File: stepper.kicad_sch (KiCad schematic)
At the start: 10 parts, among them M3 Stepper_Motor_bipolar, U2 DRV8424RGER

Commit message: schem: set stepper driver microstepping and decay config
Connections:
- net +3V3: now also U2.13 (M0)
- net GND: now also U2.15 (DECAY1), U2.16 (DECAY0)
- no-connect marks 0 -> 2
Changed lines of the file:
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@@
+	)
+	(junction
+		(at 161.29 113.03)
+		(diameter 0)
+		(color 0 0 0 0)
 	)
 	(junction
@@
 		(color 0 0 0 0)
 	)
+	(no_connect
+		(at 160.02 107.95)
+	)
+	(no_connect
+		(at 134.62 110.49)
+	)
 	(wire
 		(pts
@@
 	(wire
 		(pts
+			(xy 161.29 114.3) (xy 161.29 113.03)
+		)
+		(stroke
+			(width 0)
+			(type default)
+		)
+	)
+	(wire
+		(pts
 			(xy 125.73 91.44) (xy 125.73 92.71)
 		)
@@
 	(wire
 		(pts
+			(xy 134.62 107.95) (xy 125.73 107.95)
+		)
+		(stroke
+			(width 0)
+			(type default)
+		)
+	)
+	(wire
+		(pts
 			(xy 128.27 104.14) (xy 134.62 104.14)
 		)
@@
 	(wire
 		(pts
+			(xy 161.29 110.49) (xy 161.29 113.03)
+		)
+		(stroke
+			(width 0)
+			(type default)
+		)
+	)
+	(wire
+		(pts
 			(xy 160.02 105.41) (xy 165.1 105.41)
 		)
@@
 	(wire
 		(pts
+			(xy 125.73 107.95) (xy 125.73 106.68)
+		)
+		(stroke
+			(width 0)
+			(type default)
+		)
+	)
+	(wire
+		(pts
 			(xy 160.02 99.06) (xy 162.56 99.06)
 		)
@@
 	(wire
 		(pts
+			(xy 161.29 113.03) (xy 160.02 113.03)
+		)
+		(stroke
+			(width 0)
+			(type default)
+		)
+	)
+	(wire
+		(pts
 			(xy 146.05 80.01) (xy 146.05 78.74)
 		)
@@
 		(pts
 			(xy 172.72 101.6) (xy 172.72 99.06)
+		)
+		(stroke
+			(width 0)
+			(type default)
+		)
+	)
+	(wire
+		(pts
+			(xy 160.02 110.49) (xy 161.29 110.49)
 		)
 		(stroke
@@
 	)
 	(symbol
+		(lib_id "power:GND")
+		(at 161.29 114.3 0)
+		(mirror y)
+		(unit 1)
+		(exclude_from_sim no)
+		(in_bom yes)
+		(on_board yes)
+		(dnp no)
+		(property "Reference" "#PWR066"
+			(at 161.29 120.65 0)
+			(effects
+				(font
+					(size 1.27 1.27)
+				)
+				(hide yes)
+			)
+		)
+		(property "Value" "GND"
+			(at 165.354 115.824 0)
+			(effects
+				(font
+					(size 1.27 1.27)
+				)
+				(hide yes)
+			)
+		)
+		(property "Footprint" ""
+			(at 161.29 114.3 0)
+			(effects
+				(font
+					(size 1.27 1.27)
+				)
+				(hide yes)
+			)
+		)
+		(property "Datasheet" ""
+			(at 161.29 114.3 0)
+			(effects
+				(font
+					(size 1.27 1.27)
+				)
+				(hide yes)
+			)
+		)
+		(property "Description" "Power symbol creates a global label with name \"GND\" , ground"
+			(at 161.29 114.3 0)
+			(effects
+				(font
+					(size 1.27 1.27)
+				)
+				(hide yes)
+			)
+		)
+		(pin "1"
+		)
+		(instances
+			(project "valrob-pami-cdf-1"
+				(path "/453def7e-2a78-4c3c-a4b7-f12883e5bdd2/ac36a521-9363-451f-b288-e4e7fa573403"
+					(reference "#PWR066")
+					(unit 1)
+				)
+			)
+		)
+	)
+	(symbol
 		(lib_id "Device:C_Polarized")
 		(at 163.83 80.01 0)
@@
 					(unit 1)
 				)
+			)
+		)
+	)
+	(symbol
+		(lib_id "power:+3V3")
+		(at 125.73 106.68 0)
+		(unit 1)
+		(exclude_from_sim no)
+		(in_bom yes)
+		(on_board yes)
+		(dnp no)
+		(property "Reference" "#PWR061"
+			(at 125.73 110.49 0)
+			(effects
+				(font
+					(size 1.27 1.27)
+				)
+				(hide yes)
+			)
+		)
+		(property "Value" "+3V3"
+			(at 121.666 104.902 0)
+			(effects
+				(font
+					(size 1.27 1.27)
+				)
+			)
+		)
+		(property "Footprint" ""
+			(at 125.73 106.68 0)
+			(effects
+				(font
+					(size 1.27 1.27)
+				)
+				(hide yes)
+			)
+		)
+		(property "Datasheet" ""
+			(at 125.73 106.68 0)
+			(effects
+				(font
+					(size 1.27 1.27)
+				)
+				(hide yes)
+			)
+		)
+		(property "Description" "Power symbol creates a global label with name \"+3V3\""
+			(at 125.73 106.68 0)
+			(effects
+				(font
+					(size 1.27 1.27)
+				)
+				(hide yes)
+			)
+		)
+		(pin "1"
+		)
+		(instances
+			(project "valrob-pami-cdf-1"
+				(path "/453def7e-2a78-4c3c-a4b7-f12883e5bdd2/ac36a521-9363-451f-b288-e4e7fa573403"
+					(reference "#PWR061")
+					(unit 1)
+				)

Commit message: schem: change stepper driver connector
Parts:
- M3: footprint GLCS:JST_XH_S6B-XH-A_Stepper_1x06_P2.50mm_Horizontal -> Connector_JST:JST_XH_B4B-XH-A_1x04_P2.50mm_Vertical
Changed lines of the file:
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@@
 			)
 		)
-		(property "Footprint" "GLCS:JST_XH_S6B-XH-A_Stepper_1x06_P2.50mm_Horizontal"
+		(property "Footprint" "Connector_JST:JST_XH_B4B-XH-A_1x04_P2.50mm_Vertical"
 			(at 170.434 91.186 0)
 			(effects

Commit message: schem: fix stepper hierachical sheets
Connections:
- net ~{FAULT}: now reaches R19.1, U2.11 (~{FAULT})
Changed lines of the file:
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@@
+	)
+	(junction
+		(at 125.73 101.6)
+		(diameter 0)
+		(color 0 0 0 0)
 	)
 	(junction
@@
 	(wire
 		(pts
+			(xy 124.46 101.6) (xy 125.73 101.6)
+		)
+		(stroke
+			(width 0)
+			(type default)
+		)
+	)
+	(wire
+		(pts
 			(xy 147.32 123.19) (xy 147.32 124.46)
 		)
@@
 	(wire
 		(pts
-			(xy 129.54 93.98) (xy 134.62 93.98)
-		)
-		(stroke
-			(width 0)
-			(type default)
-		)
-	)
-	(wire
-		(pts
 			(xy 161.29 88.9) (xy 161.29 91.44)
 		)
@@
 	(wire
 		(pts
+			(xy 133.35 91.44) (xy 134.62 91.44)
+		)
+		(stroke
+			(width 0)
+			(type default)
+		)
+	)
+	(wire
+		(pts
 			(xy 163.83 96.52) (xy 160.02 96.52)
 		)
@@
 	(wire
 		(pts
-			(xy 128.27 104.14) (xy 134.62 104.14)
-		)
-		(stroke
-			(width 0)
-			(type default)
-		)
-	)
-	(wire
-		(pts
-			(xy 129.54 96.52) (xy 134.62 96.52)
-		)
-		(stroke
-			(width 0)
-			(type default)
-		)
-	)
-	(wire
-		(pts
 			(xy 167.64 105.41) (xy 167.64 106.68)
 		)
@@
 	(wire
 		(pts
+			(xy 133.35 93.98) (xy 134.62 93.98)
+		)
+		(stroke
+			(width 0)
+			(type default)
+		)
+	)
+	(wire
+		(pts
 			(xy 161.29 110.49) (xy 161.29 113.03)
 		)
@@
 	(wire
 		(pts
+			(xy 133.35 96.52) (xy 134.62 96.52)
+		)
+		(stroke
+			(width 0)
+			(type default)
+		)
+	)
+	(wire
+		(pts
 			(xy 148.59 74.93) (xy 153.67 74.93)
 		)
@@
 	(wire
 		(pts
-			(xy 176.53 105.41) (xy 182.88 105.41)
-		)
-		(stroke
-			(width 0)
-			(type default)
-		)
-	)
-	(wire
-		(pts
-			(xy 129.54 91.44) (xy 134.62 91.44)
+			(xy 176.53 105.41) (xy 179.07 105.41)
 		)
 		(stroke
@@
 		)
 	)
-	(label "STEP"
-		(at 129.54 91.44 0)
+	(hierarchical_label "~{SLEEP}"
+		(shape input)
+		(at 134.62 104.14 180)
 		(effects
 			(font
 				(size 1.27 1.27)
 			)
-			(justify left bottom)
-		)
-	)
-	(label "~{SLEEP}"
-		(at 128.27 104.14 0)
+			(justify right)
+		)
+	)
+	(hierarchical_label "DIR"
+		(shape input)
+		(at 133.35 93.98 180)
 		(effects
 			(font
 				(size 1.27 1.27)
 			)
-			(justify left bottom)
-		)
-	)
-	(label "VPWM"
-		(at 182.88 105.41 180)
+			(justify right)
+		)
+	)
+	(hierarchical_label "STEP"
+		(shape input)
+		(at 133.35 91.44 180)
 		(effects
 			(font
 				(size 1.27 1.27)
 			)
-			(justify right bottom)
-		)
-	)
-	(label "EN"
-		(at 129.54 96.52 0)
+			(justify right)
+		)
+	)
+	(hierarchical_label "~{FAULT}"
+		(shape output)
+		(at 124.46 101.6 180)
 		(effects
 			(font
 				(size 1.27 1.27)
 			)
-			(justify left bottom)
-		)
-	)
-	(label "DIR"
-		(at 129.54 93.98 0)
+			(justify right)
+		)
+	)
+	(hierarchical_label "EN"
+		(shape input)
+		(at 133.35 96.52 180)
 		(effects
 			(font
 				(size 1.27 1.27)
 			)
-			(justify left bottom)
+			(justify right)
+		)
+	)
+	(hierarchical_label "VPWM"
+		(shape input)
+		(at 179.07 105.41 0)
+		(effects
+			(font
+				(size 1.27 1.27)
+			)
+			(justify left)
 		)
 	)
@@
 				(path "/453def7e-2a78-4c3c-a4b7-f12883e5bdd2/ac36a521-9363-451f-b288-e4e7fa573403"
 					(reference "#PWR049")
+					(unit 1)
+				)
+				(path "/453def7e-2a78-4c3c-a4b7-f12883e5bdd2/da99261a-b7a2-4c14-91bb-816ce46ae8f8"
+					(reference "#PWR077")
 					(unit 1)
 				)
@@
 					(unit 1)
 				)
+				(path "/453def7e-2a78-4c3c-a4b7-f12883e5bdd2/da99261a-b7a2-4c14-91bb-816ce46ae8f8"
+					(reference "C40")
+					(unit 1)
+				)
 			)
 		)
@@
 					(unit 1)
 				)
+				(path "/453def7e-2a78-4c3c-a4b7-f12883e5bdd2/da99261a-b7a2-4c14-91bb-816ce46ae8f8"
+					(reference "#PWR074")
+					(unit 1)
+				)
 			)
 		)
@@
 					(unit 1)
 				)
+				(path "/453def7e-2a78-4c3c-a4b7-f12883e5bdd2/da99261a-b7a2-4c14-91bb-816ce46ae8f8"
+					(reference "C39")
+					(unit 1)
+				)
 			)
 		)
@@
 					(unit 1)
 				)
+				(path "/453def7e-2a78-4c3c-a4b7-f12883e5bdd2/da99261a-b7a2-4c14-91bb-816ce46ae8f8"
+					(reference "#PWR069")
+					(unit 1)
+				)
 			)
 		)
@@
 					(unit 1)
 				)
+				(path "/453def7e-2a78-4c3c-a4b7-f12883e5bdd2/da99261a-b7a2-4c14-91bb-816ce46ae8f8"
+					(reference "M2")
+					(unit 1)
+				)
 			)
 		)
@@
 					(unit 1)
 				)
+				(path "/453def7e-2a78-4c3c-a4b7-f12883e5bdd2/da99261a-b7a2-4c14-91bb-816ce46ae8f8"
+					(reference "#PWR072")
+					(unit 1)
+				)
 			)
 		)
@@
 				(path "/453def7e-2a78-4c3c-a4b7-f12883e5bdd2/ac36a521-9363-451f-b288-e4e7fa573403"
 					(reference "#PWR01")
+					(unit 1)
+				)
+				(path "/453def7e-2a78-4c3c-a4b7-f12883e5bdd2/da99261a-b7a2-4c14-91bb-816ce46ae8f8"
+					(reference "#PWR067")
 					(unit 1)
 				)
@@
 				(path "/453def7e-2a78-4c3c-a4b7-f12883e5bdd2/ac36a521-9363-451f-b288-e4e7fa573403"
 					(reference "#PWR023")
+					(unit 1)
+				)
+				(path "/453def7e-2a78-4c3c-a4b7-f12883e5bdd2/da99261a-b7a2-4c14-91bb-816ce46ae8f8"
+					(reference "#PWR073")
 					(unit 1)
 				)
@@
 					(unit 1)
 				)
+				(path "/453def7e-2a78-4c3c-a4b7-f12883e5bdd2/da99261a-b7a2-4c14-91bb-816ce46ae8f8"
+					(reference "R33")
+					(unit 1)
+				)
 			)
 		)
@@
 					(unit 1)
 				)
+				(path "/453def7e-2a78-4c3c-a4b7-f12883e5bdd2/da99261a-b7a2-4c14-91bb-816ce46ae8f8"
+					(reference "#FLG08")
+					(unit 1)
+				)
 			)
 		)
@@
 					(unit 1)
 				)
+				(path "/453def7e-2a78-4c3c-a4b7-f12883e5bdd2/da99261a-b7a2-4c14-91bb-816ce46ae8f8"
+					(reference "C36")
+					(unit 1)
+				)
 			)
 		)
@@
 					(unit 1)
 				)
+				(path "/453def7e-2a78-4c3c-a4b7-f12883e5bdd2/da99261a-b7a2-4c14-91bb-816ce46ae8f8"
+					(reference "#PWR075")
+					(unit 1)
+				)
 			)
 		)
@@
 				(path "/453def7e-2a78-4c3c-a4b7-f12883e5bdd2/ac36a521-9363-451f-b288-e4e7fa573403"
 					(reference "C30")
+					(unit 1)
+				)
+				(path "/453def7e-2a78-4c3c-a4b7-f12883e5bdd2/da99261a-b7a2-4c14-91bb-816ce46ae8f8"
+					(reference "C37")
 					(unit 1)
 				)
@@
 					(unit 1)
 				)
+				(path "/453def7e-2a78-4c3c-a4b7-f12883e5bdd2/da99261a-b7a2-4c14-91bb-816ce46ae8f8"
+					(reference "#PWR076")
+					(unit 1)
+				)
 			)
 		)
@@
 					(unit 1)
 				)
+				(path "/453def7e-2a78-4c3c-a4b7-f12883e5bdd2/da99261a-b7a2-4c14-91bb-816ce46ae8f8"
+					(reference "C35")
+					(unit 1)
+				)
 			)
 		)
@@
 					(unit 1)
 				)
+				(path "/453def7e-2a78-4c3c-a4b7-f12883e5bdd2/da99261a-b7a2-4c14-91bb-816ce46ae8f8"
+					(reference "C38")
+					(unit 1)
+				)
 			)
 		)
@@
 					(unit 1)
 				)
+				(path "/453def7e-2a78-4c3c-a4b7-f12883e5bdd2/da99261a-b7a2-4c14-91bb-816ce46ae8f8"
+					(reference "U6")
+					(unit 1)
+				)
 			)
 		)
@@
 					(unit 1)
 				)
+				(path "/453def7e-2a78-4c3c-a4b7-f12883e5bdd2/da99261a-b7a2-4c14-91bb-816ce46ae8f8"
+					(reference "R34")
+					(unit 1)
+				)

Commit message: schem: reannotate
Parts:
- renumbered C28 to C35, C29 to C36, C30 to C37, C31 to C38, C32 to C39, C33 to C40, M3 to M2, R19 to R36, R27 to R37, U2 to U6

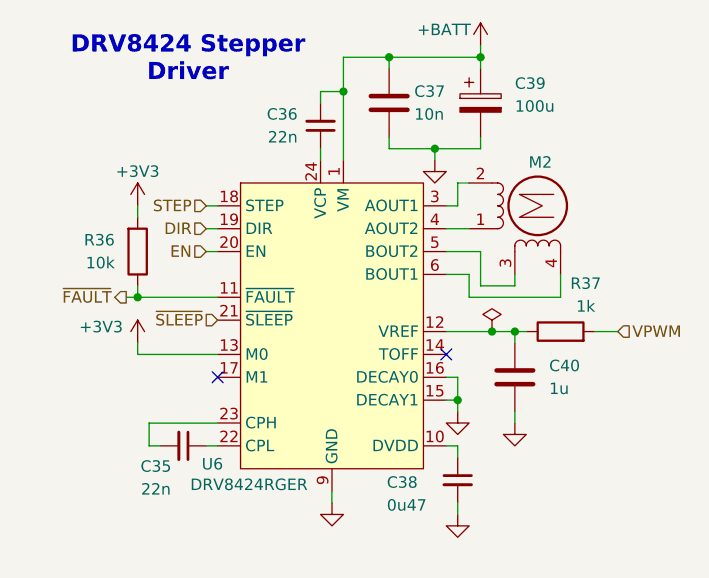
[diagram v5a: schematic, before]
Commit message: pcb: add stepper layout
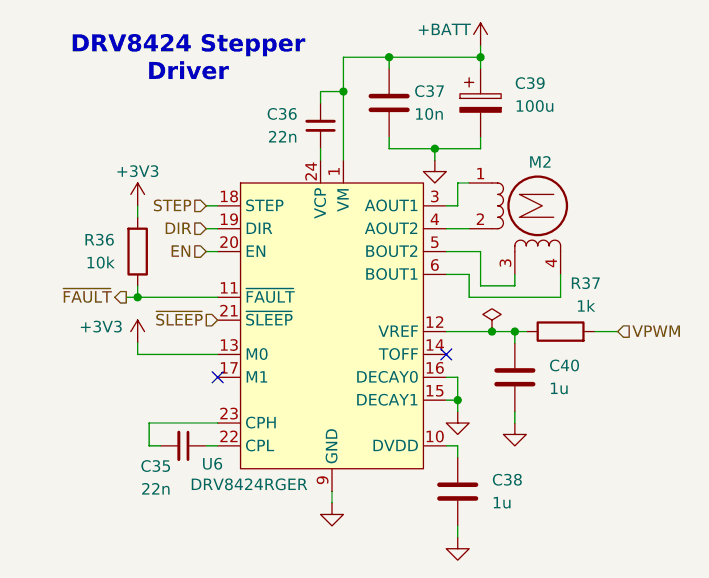
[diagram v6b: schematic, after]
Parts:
- removed C38: 0u47, Capacitor_SMD:C_0603_1608Metric, symbol Device:C_Small
- added C38: 1u, Capacitor_SMD:C_0402_1005Metric, symbol Device:C
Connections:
- net GND: now also C38.2
- net at M2.1 (-): now also U6.3 (AOUT1); no longer U6.4 (AOUT2)
- net at M2.2: now also U6.4 (AOUT2); no longer U6.3 (AOUT1)
- net at U6.10 (DVDD): now also C38.1
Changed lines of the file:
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@@
 	(wire
 		(pts
-			(xy 161.29 124.46) (xy 161.29 125.73)
+			(xy 161.29 127) (xy 161.29 128.27)
 		)
 		(stroke
@@
 	(symbol
 		(lib_id "power:GND")
-		(at 161.29 125.73 0)
+		(at 161.29 128.27 0)
 		(unit 1)
 		(exclude_from_sim no)
@@
 		(dnp no)
 		(property "Reference" "#PWR083"
-			(at 161.29 132.08 0)
+			(at 161.29 134.62 0)
 			(effects
 				(font
@@
 		)
 		(property "Value" "GND"
-			(at 157.226 127.254 0)
+			(at 157.226 129.794 0)
 			(effects
 				(font
@@
 		)
 		(property "Footprint" ""
-			(at 161.29 125.73 0)
+			(at 161.29 128.27 0)
 			(effects
 				(font
@@
 		)
 		(property "Datasheet" ""
-			(at 161.29 125.73 0)
+			(at 161.29 128.27 0)
 			(effects
 				(font
@@
 		)
 		(property "Description" "Power symbol creates a global label with name \"GND\" , ground"
-			(at 161.29 125.73 0)
+			(at 161.29 128.27 0)
 			(effects
 				(font
@@
 	)
 	(symbol
-		(lib_id "Device:C_Small")
-		(at 161.29 121.92 0)
+		(lib_id "Device:C")
+		(at 161.29 123.19 0)
+		(mirror y)
 		(unit 1)
 		(exclude_from_sim no)
@@
 		(on_board yes)
 		(dnp no)
+		(fields_autoplaced yes)
 		(property "Reference" "C38"
-			(at 153.416 122.174 0)
-			(effects
-				(font
-					(size 1.27 1.27)
-				)
-				(justify left)
-			)
-		)
-		(property "Value" "0u47"
-			(at 153.416 124.714 0)
-			(effects
-				(font
-					(size 1.27 1.27)
-				)
-				(justify left)
-			)
-		)
-		(property "Footprint" "Capacitor_SMD:C_0603_1608Metric"
-			(at 161.29 121.92 0)
+			(at 165.1 121.9199 0)
+			(effects
+				(font
+					(size 1.27 1.27)
+				)
+				(justify right)
+			)
+		)
+		(property "Value" "1u"
+			(at 165.1 124.4599 0)
+			(effects
+				(font
+					(size 1.27 1.27)
+				)
+				(justify right)
+			)
+		)
+		(property "Footprint" "Capacitor_SMD:C_0402_1005Metric"
+			(at 160.3248 127 0)
 			(effects
 				(font
@@
 		)
 		(property "Datasheet" "~"
-			(at 161.29 121.92 0)
-			(effects
-				(font
-					(size 1.27 1.27)
-				)
-				(hide yes)
-			)
-		)
-		(property "Description" "Unpolarized capacitor, small symbol"
-			(at 161.29 121.92 0)
+			(at 161.29 123.19 0)
+			(effects
+				(font
+					(size 1.27 1.27)
+				)
+				(hide yes)
+			)
+		)
+		(property "Description" "Unpolarized capacitor"
+			(at 161.29 123.19 0)
 			(effects
 				(font
@@
 		)
 		(property "Basic" "Y"
-			(at 161.29 121.92 0)
-			(effects
-				(font
-					(size 1.27 1.27)
-				)
-				(hide yes)
-			)
-		)
-		(property "JLCPCB Part #" "C1623"
-			(at 161.29 121.92 0)
+			(at 161.29 123.19 0)
+			(effects
+				(font
+					(size 1.27 1.27)
+				)
+				(hide yes)
+			)
+		)
+		(property "JLCPCB Part #" "C52923"
+			(at 161.29 123.19 0)
 			(effects
 				(font
@@
 		)
 		(property "Manufacturer" "Samsung Electro-Mechanics "
-			(at 161.29 121.92 0)
-			(effects
-				(font
-					(size 1.27 1.27)
-				)
-				(hide yes)
-			)
-		)
-		(property "Manufacturer Part Number" "CL10B474KA8NNNC"
-			(at 161.29 121.92 0)
-			(effects
-				(font
+			(at 161.29 123.19 0)
+			(effects
+				(font
+					(size 1.27 1.27)
+				)
+				(hide yes)
+			)
+		)
+		(property "Manufacturer Part Number" "CL05A105KA5NQNC"
+			(at 161.29 123.19 0)
+			(effects
+				(font

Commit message: schem: update connectors to horizontal footprints
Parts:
- M2: footprint Connector_JST:JST_XH_B4B-XH-A_1x04_P2.50mm_Vertical -> Connector_JST:JST_XH_S4B-XH-A_1x04_P2.50mm_Horizontal
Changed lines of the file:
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@@
 			)
 		)
-		(property "Footprint" "Connector_JST:JST_XH_B4B-XH-A_1x04_P2.50mm_Vertical"
+		(property "Footprint" "Connector_JST:JST_XH_S4B-XH-A_1x04_P2.50mm_Horizontal"
 			(at 170.434 91.186 0)
 			(effects

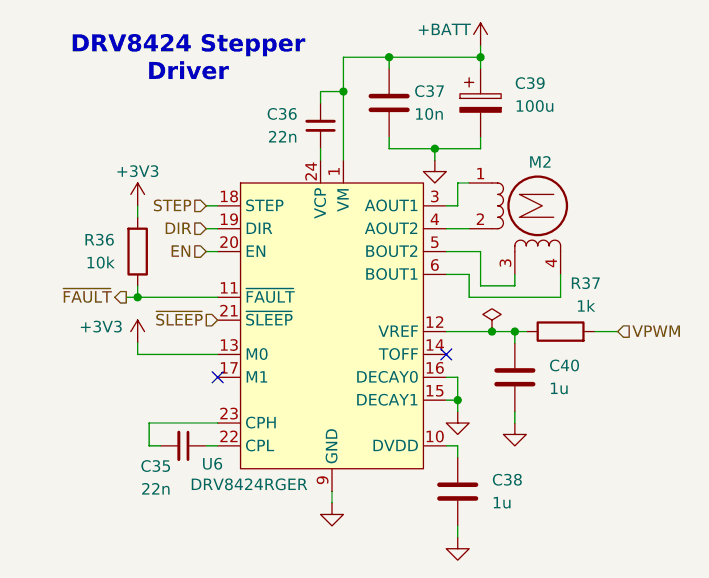
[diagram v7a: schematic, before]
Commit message: pcb: add local stepper drivers routing
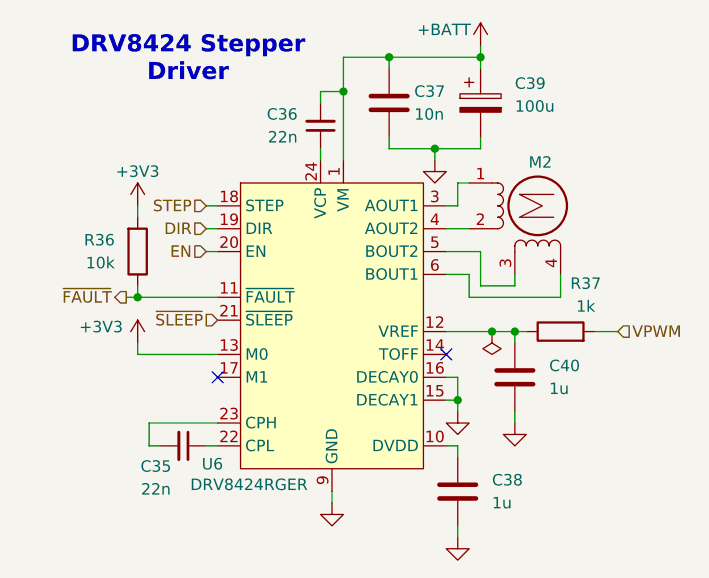
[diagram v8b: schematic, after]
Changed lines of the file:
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@@
+	(wire
+		(pts
+			(xy 160.02 105.41) (xy 165.1 105.41)
+		)
+		(stroke
+			(width 0)
+			(type default)
+		)
+	)
 	(wire
 		(pts
@@
 	(wire
 		(pts
-			(xy 160.02 105.41) (xy 165.1 105.41)
-		)
-		(stroke
-			(width 0)
-			(type default)
-		)
-	)
-	(wire
-		(pts
 			(xy 133.35 96.52) (xy 134.62 96.52)
 		)
@@
 	(wire
 		(pts
+			(xy 161.29 119.38) (xy 161.29 118.11)
+		)
+		(stroke
+			(width 0)
+			(type default)
+		)
+	)
+	(wire
+		(pts
+			(xy 163.83 74.93) (xy 153.67 74.93)
+		)
+		(stroke
+			(width 0)
+			(type default)
+		)
+	)
+	(wire
+		(pts
+			(xy 161.29 118.11) (xy 160.02 118.11)
+		)
+		(stroke
+			(width 0)
+			(type default)
+		)
+	)
+	(wire
+		(pts
+			(xy 148.59 86.36) (xy 148.59 78.74)
+		)
+		(stroke
+			(width 0)
+			(type default)
+		)
+	)
+	(wire
+		(pts
+			(xy 172.72 101.6) (xy 172.72 99.06)
+		)
+		(stroke
+			(width 0)
+			(type default)
+		)
+	)
+	(wire
+		(pts
+			(xy 160.02 110.49) (xy 161.29 110.49)
+		)
+		(stroke
+			(width 0)
+			(type default)
+		)
+	)
+	(wire
+		(pts
+			(xy 176.53 105.41) (xy 179.07 105.41)
+		)
+		(stroke
+			(width 0)
+			(type default)
+		)
+	)
+	(wire
+		(pts
+			(xy 161.29 127) (xy 161.29 128.27)
+		)
+		(stroke
+			(width 0)
+			(type default)
+		)
+	)
+	(wire
+		(pts
+			(xy 158.75 85.09) (xy 158.75 86.36)
+		)
+		(stroke
+			(width 0)
+			(type default)
+		)
+	)
+	(wire
+		(pts
+			(xy 160.02 93.98) (xy 162.56 93.98)
+		)
+		(stroke
+			(width 0)
+			(type default)
+		)
+	)
+	(wire
+		(pts
+			(xy 153.67 85.09) (xy 158.75 85.09)
+		)
+		(stroke
+			(width 0)
+			(type default)
+		)
+	)
+	(wire
+		(pts
 			(xy 165.1 105.41) (xy 167.64 105.41)
-		)
-		(stroke
-			(width 0)
-			(type default)
-		)
-	)
-	(wire
-		(pts
-			(xy 161.29 119.38) (xy 161.29 118.11)
-		)
-		(stroke
-			(width 0)
-			(type default)
-		)
-	)
-	(wire
-		(pts
-			(xy 163.83 74.93) (xy 153.67 74.93)
-		)
-		(stroke
-			(width 0)
-			(type default)
-		)
-	)
-	(wire
-		(pts
-			(xy 161.29 118.11) (xy 160.02 118.11)
-		)
-		(stroke
-			(width 0)
-			(type default)
-		)
-	)
-	(wire
-		(pts
-			(xy 148.59 86.36) (xy 148.59 78.74)
-		)
-		(stroke
-			(width 0)
-			(type default)
-		)
-	)
-	(wire
-		(pts
-			(xy 172.72 101.6) (xy 172.72 99.06)
-		)
-		(stroke
-			(width 0)
-			(type default)
-		)
-	)
-	(wire
-		(pts
-			(xy 160.02 110.49) (xy 161.29 110.49)
-		)
-		(stroke
-			(width 0)
-			(type default)
-		)
-	)
-	(wire
-		(pts
-			(xy 176.53 105.41) (xy 179.07 105.41)
-		)
-		(stroke
-			(width 0)
-			(type default)
-		)
-	)
-	(wire
-		(pts
-			(xy 161.29 127) (xy 161.29 128.27)
-		)
-		(stroke
-			(width 0)
-			(type default)
-		)
-	)
-	(wire
-		(pts
-			(xy 158.75 85.09) (xy 158.75 86.36)
-		)
-		(stroke
-			(width 0)
-			(type default)
-		)
-	)
-	(wire
-		(pts
-			(xy 160.02 93.98) (xy 162.56 93.98)
-		)
-		(stroke
-			(width 0)
-			(type default)
-		)
-	)
-	(wire
-		(pts
-			(xy 153.67 85.09) (xy 158.75 85.09)
 		)
 		(stroke
@@
 	(symbol
 		(lib_id "power:PWR_FLAG")
-		(at 165.1 105.41 0)
+		(at 165.1 105.41 180)
 		(unit 1)
 		(exclude_from_sim no)
@@
 		(fields_autoplaced yes)
 		(property "Reference" "#FLG06"
-			(at 165.1 103.505 0)
+			(at 165.1 107.315 0)
 			(effects
 				(font
@@
 		)
 		(property "Value" "PWR_FLAG"
-			(at 165.1 100.33 0)
-			(effects
-				(font
+			(at 165.1 110.49 0)
+			(effects
+				(font
